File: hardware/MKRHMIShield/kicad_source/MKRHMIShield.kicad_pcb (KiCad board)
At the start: 2 copper layers, 72 x 53 mm, 29 parts, among them CN1 ARDUINO_MKR, Q1 2N7002, SW1 TAST_VER, SW2 TAST_VER, SW3 TAST_VER, SW4 TAST_VER, SW5 TAST_VER, SW6 TAST_VER

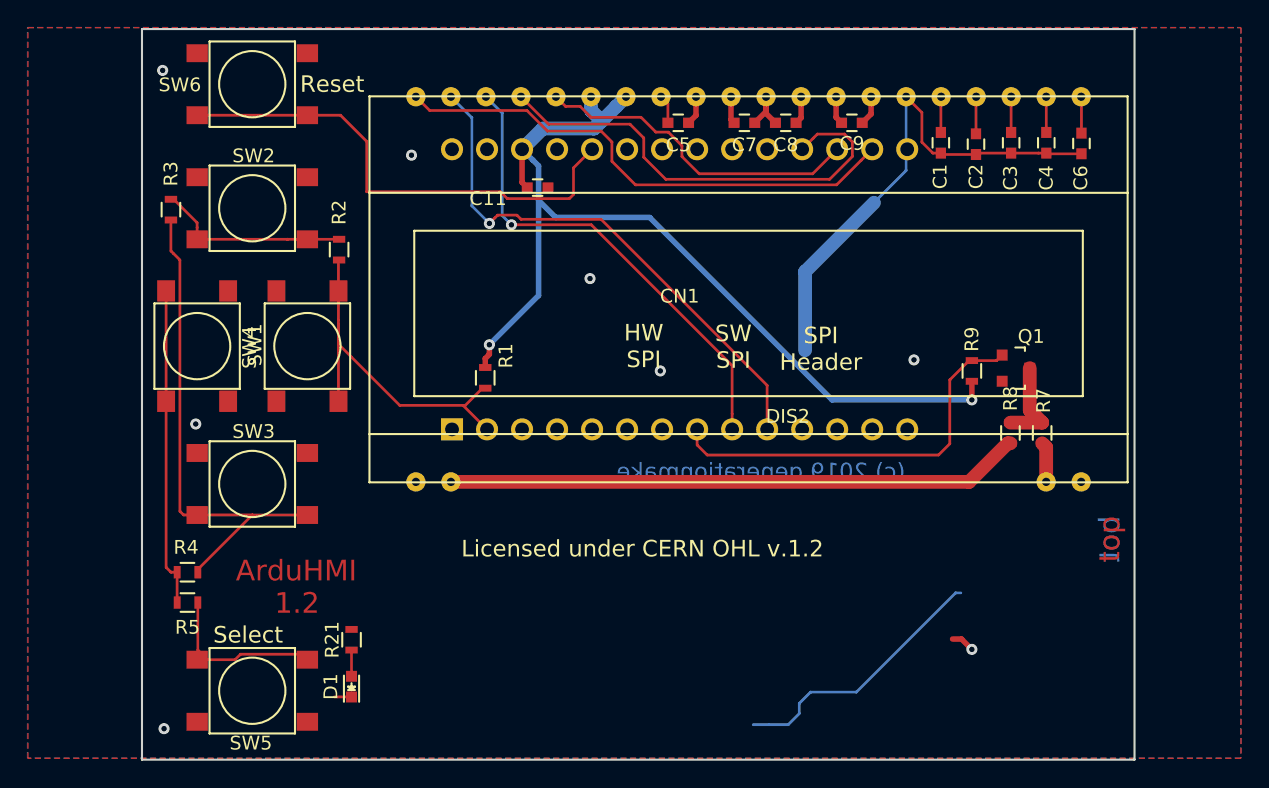
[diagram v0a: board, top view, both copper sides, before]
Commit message: exchanged switches with a joystick
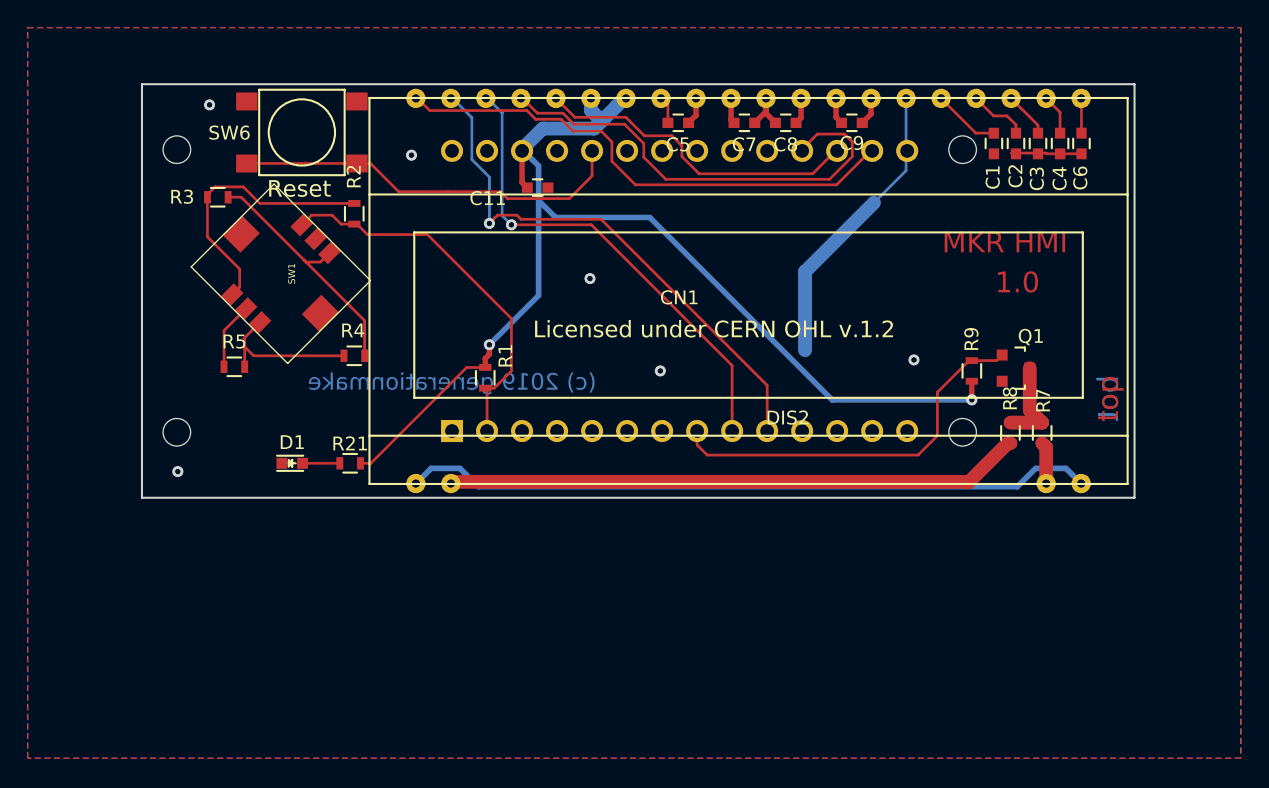
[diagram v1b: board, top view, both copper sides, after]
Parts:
- removed SW2, SW3, SW4, SW5: TAST_VER, mechanical-switches:WE_430182080816
- CN1: footprint MODULE_compute:ARDUINO_MKR -> MODULE_compute:ARDUINO_MKR_HOLES
- SW1: value TAST_VER -> ALPS_SKRH; footprint mechanical-switches:WE_430182080816 -> mechanical-switches:ALPS_SKRH
- moved R4 19.8 mm to (66.4, 100.7)
- moved R5 17.4 mm to (57.7, 101.5), turned to 180 degrees
- moved D1 16.8 mm to (61.9, 108.5), turned to 0 degrees
- moved R21 12.8 mm to (66.1, 108.5), turned to 0 degrees
- moved SW6 5.02 mm to (62.6, 84.5)
- moved C1 3.85 mm to (112.8, 85.3)
- moved R3 3.52 mm to (56.5, 89.2), turned to 0 degrees
- moved C2 2.90 mm to (114.4, 85.3)
- moved R2 2.82 mm to (66.4, 90.4)
- moved C3 1.95 mm to (116.0, 85.3)
- moved C4 1.00 mm to (117.6, 85.3)
- moved SW1 1.00 mm to (63.0, 99.0)
- moved CN1 0.12 mm to (90.0, 96.0)
- moved DIS2 0.12 mm to (95.0, 96.0)
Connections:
- SW1 pad 1: GND -> /BUTTON_UP
- SW1 pad 2: /KEYPAD_A0 -> /BUTTON_SELECT
- SW1 pad 3: GND -> /BUTTON_LEFT
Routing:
- net +5V: track 0.00 -> 50.3 mm
- net GND: track 61.7 -> 28.6 mm, vias 8 -> 6
- net /BUTTON_DOWN: track 35.8 -> 18.4 mm
- net /BUTTON_LEFT: track 23.2 -> 11.1 mm
- net +3V3: track 70.9 -> 82.8 mm
- net /RESET: track 35.9 -> 28.6 mm
- net /BUTTON_SELECT: track 12.0 -> 4.88 mm
- net /BUTTON_UP: track 14.1 -> 19.8 mm
- net /DIS_V4: track 2.60 -> 4.90 mm
- net /DIS_V3: track 2.69 -> 4.30 mm
- net /DISPLAY_BL: track 29.3 -> 28.4 mm
- net Net-(D1-Pad2): track 1.90 -> 2.70 mm
- net /DIS_V2: track 2.59 -> 3.33 mm
- net /KEYPAD_A0: track 27.2 -> 27.9 mm
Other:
- board size 72 x 53 mm -> 72 x 30 mm
- board text added: "1.0"
- board text added: "MKR HMI"
- board text added: "for EA DOGM132-5"
- board text removed: "1.2"
- board text removed: "HW SPI"
- board text removed: "SPI Header"
- board text removed: "SW SPI"
- board text removed: "Select"
- board text removed: "for EA DOGS102-6 EA DOGM132-5 EA DOGM128-6"
